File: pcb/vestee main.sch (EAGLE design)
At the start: 45 parts, among them IC1 LD117AS12TR, IC2 FT232RL, Q1 MMBT2222A, Q3 MMBT4403

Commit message: Fixed discovered issues, removed DC jack, added jack for 1-Wire, minor improvements
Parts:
- removed D1, D2: (no value), SparkFun-DiscreteSemi:DIODESMA
- removed JP1: USB-SMD-NS, SparkFun-Connectors:USB-SMD-NS
- removed R17: (no value), rcl:R-EU_R0805
- removed SENS: (no value), SparkFun-Connectors:M05LOCK_LONGPADS
- removed U$3: TACTILE-SWITCH-PTH, GeekAmmo:TACTILE-SWITCH-PTH
- removed VESTEE: (no value), SparkFun-Connectors:M04LOCK_LONGPADS
- added ELECTRODE: (no value), SparkFun-Connectors:M02LOCK_LONGPADS
- added PRPIHERALS: (no value), SparkFun-Connectors:AUDIO-JACK1:1
- added Q2, Q4: MMBT5088, SparkFun-DiscreteSemi:TRANSISTOR_NPNMMBT5088
- added R22, R23, R24, R25: (no value), rcl:R-EU_R0805
- added S2: SWITCH-MOMENTARY-2SMD-4, SparkFun-Electromechanical:SWITCH-MOMENTARY-2SMD-4
- JP2: value 5.5x2.1mm Barrel -> USB-MICROB; device SparkFun-Connectors:POWER_JACKSMD -> SparkFun-Connectors:USB-MICROB
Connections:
- removed net FLOW: R17.2, U$1.GPIO13
- removed net N$20: R12.1, SENS.2
- removed net N$22: R11.1, U$1.REST
- removed net N$23: C4.1, D2.A, IC2.VCC, L1.2
- removed net N$24: U$1.GPIO12, VESTEE.3
- removed net N$25: Q3.C, SENS.5
- removed net N$5: R17.1, VESTEE.4
- new net 1-WIRE: PRPIHERALS.LEFT, R12.1
- new net CBUS_RST: R11.1, R25.2, U$1.REST
- new net N$30: IC2.CBUS2, R22.2
- new net N$31: Q2.C, R24.1
- new net N$32: Q2.B, R23.1
- new net N$33: Q4.B, R22.1
- new net N$34: IC2.CBUS3, R23.2
- new net N$35: Q4.C, R25.1
- net CBUS: now also R24.2; no longer IC2.CBUS4, U$1.GPIO15
- net GND: now also IC2.TEST, JP2.GND, PRPIHERALS.SLEEVE, Q2.E, Q4.E, S2.1, U$1.GPIO15; no longer JP1.GND, JP2.PWR, SENS.1, U$3.1, U$3.2, VESTEE.1
- net N$17: now also ELECTRODE.1, Q3.C; no longer D1.A, JP2.GND, JP2.GNDBREAK
- net N$18: now also S2.2; no longer U$3.3, U$3.4
- net N$2: now also JP2.D+; no longer JP1.D+
- net N$26: now also ELECTRODE.2; no longer SENS.4
- net N$3: now also JP2.D-; no longer JP1.D-
- net N$7: now also JP2.VBUS; no longer JP1.VBUS
- net VCC: now also PRPIHERALS.RIGHT; no longer SENS.3, VESTEE.2
- net VIN: now also C4.1, IC2.VCC, L1.2; no longer D1.C, D2.C

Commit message: Fixed silkscreen
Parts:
- renumbered LED1 to TX, LED2 to RX, LED3 to 3V3
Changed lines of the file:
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@@
 <part name="R3" library="rcl" deviceset="R-EU_" device="R0805"/>
 <part name="R4" library="rcl" deviceset="R-EU_" device="R0805"/>
-<part name="LED1" library="led" deviceset="LED" device="SML0805"/>
-<part name="LED2" library="led" deviceset="LED" device="SML0805"/>
-<part name="LED3" library="led" deviceset="LED" device="SML0805"/>
+<part name="TX" library="led" deviceset="LED" device="SML0805"/>
+<part name="RX" library="led" deviceset="LED" device="SML0805"/>
+<part name="3V3" library="led" deviceset="LED" device="SML0805"/>
 <part name="R5" library="rcl" deviceset="R-EU_" device="R0805"/>
 <part name="GND8" library="supply1" deviceset="GND" device=""/>
@@
 <instance part="R3" gate="G$1" x="170.18" y="58.42" rot="R90"/>
 <instance part="R4" gate="G$1" x="177.8" y="58.42" rot="R90"/>
-<instance part="LED1" gate="G$1" x="170.18" y="68.58"/>
-<instance part="LED2" gate="G$1" x="177.8" y="68.58"/>
-<instance part="LED3" gate="G$1" x="111.76" y="101.6"/>
+<instance part="TX" gate="G$1" x="170.18" y="68.58"/>
+<instance part="RX" gate="G$1" x="177.8" y="68.58"/>
+<instance part="3V3" gate="G$1" x="111.76" y="101.6"/>
 <instance part="R5" gate="G$1" x="104.14" y="106.68" rot="R180"/>
 <instance part="GND8" gate="1" x="111.76" y="91.44"/>
@@
 </segment>
 <segment>
-<pinref part="LED3" gate="G$1" pin="C"/>
+<pinref part="3V3" gate="G$1" pin="C"/>
 <pinref part="GND8" gate="1" pin="GND"/>
 <wire x1="111.76" y1="96.52" x2="111.76" y2="93.98" width="0.1524" layer="91"/>
@@
 <pinref part="IC2" gate="1" pin="VCCIO"/>
 <wire x1="124.46" y1="73.66" x2="129.54" y2="73.66" width="0.1524" layer="91"/>
-<pinref part="LED2" gate="G$1" pin="A"/>
+<pinref part="RX" gate="G$1" pin="A"/>
 <wire x1="177.8" y1="71.12" x2="177.8" y2="83.82" width="0.1524" layer="91"/>
 <wire x1="177.8" y1="83.82" x2="170.18" y2="83.82" width="0.1524" layer="91"/>
 <wire x1="170.18" y1="83.82" x2="124.46" y2="83.82" width="0.1524" layer="91"/>
 <wire x1="124.46" y1="83.82" x2="124.46" y2="81.28" width="0.1524" layer="91"/>
-<pinref part="LED1" gate="G$1" pin="A"/>
+<pinref part="TX" gate="G$1" pin="A"/>
 <wire x1="124.46" y1="81.28" x2="124.46" y2="73.66" width="0.1524" layer="91"/>
 <wire x1="170.18" y1="71.12" x2="170.18" y2="83.82" width="0.1524" layer="91"/>
@@
 <segment>
 <pinref part="R3" gate="G$1" pin="2"/>
-<pinref part="LED1" gate="G$1" pin="C"/>
+<pinref part="TX" gate="G$1" pin="C"/>
 </segment>
 </net>
@@
 <segment>
 <pinref part="R4" gate="G$1" pin="2"/>
-<pinref part="LED2" gate="G$1" pin="C"/>
+<pinref part="RX" gate="G$1" pin="C"/>
 </segment>
 </net>
@@
 <segment>
 <pinref part="R5" gate="G$1" pin="1"/>
-<pinref part="LED3" gate="G$1" pin="A"/>
+<pinref part="3V3" gate="G$1" pin="A"/>
 <wire x1="109.22" y1="106.68" x2="111.76" y2="106.68" width="0.1524" layer="91"/>
 <wire x1="111.76" y1="106.68" x2="111.76" y2="104.14" width="0.1524" layer="91"/>

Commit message: Added new LED to GPIO12, screw holes, bottom layer fixes
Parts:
- removed ELECTRODE: (no value), SparkFun-Connectors:M02LOCK_LONGPADS
- added LED1: (no value), led:LED3MM
- added PAD1, PAD2: (no value), wirepad:SMD2
- added Q5: MMBT5088, SparkFun-DiscreteSemi:TRANSISTOR_NPNMMBT5088
- added R17, R26: (no value), rcl:R-EU_R0805
- C2: device SparkFun-Capacitors:CAP_POLPTH2 -> SparkFun-Capacitors:CAP_POLD
- L1: device SparkFun-Passives:INDUCTOR0805 -> SparkFun-Passives:INDUCTOR1210
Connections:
- new net N$20: R17.1, U$1.GPIO12
- new net N$22: LED1.C, Q5.C
- new net N$23: LED1.A, R26.2
- new net N$5: Q5.B, R17.2
- net GND: now also Q5.E
- net N$17: now also PAD2.P; no longer ELECTRODE.1
- net N$26: now also PAD1.P; no longer ELECTRODE.2
- net VCC: now also R26.1
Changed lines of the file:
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@@
 <layer number="17" name="Pads" color="2" fill="1" visible="no" active="no"/>
 <layer number="18" name="Vias" color="2" fill="1" visible="no" active="no"/>
-<layer number="19" name="Unrouted" color="6" fill="1" visible="no" active="no"/>
+<layer number="19" name="Unrouted" color="14" fill="1" visible="no" active="no"/>
 <layer number="20" name="Dimension" color="15" fill="1" visible="no" active="no"/>
 <layer number="21" name="tPlace" color="7" fill="1" visible="no" active="no"/>
@@
 <part name="GND3" library="supply1" deviceset="GND" device=""/>
 <part name="IC1" library="v-reg" deviceset="LD117A?*" device="S" technology="12TR"/>
-<part name="C2" library="SparkFun-Capacitors" deviceset="CAP_POL" device="PTH2"/>
+<part name="C2" library="SparkFun-Capacitors" deviceset="CAP_POL" device="D"/>
 <part name="C3" library="SparkFun-Capacitors" deviceset="0.33UF-50V-10%(0805)" device="" value="100nF"/>
 <part name="GND4" library="supply1" deviceset="GND" device=""/>
@@
 <part name="R2" library="rcl" deviceset="R-EU_" device="R0805"/>
 <part name="P+2" library="supply1" deviceset="VCC" device=""/>
-<part name="L1" library="SparkFun-Passives" deviceset="INDUCTOR" device="0805"/>
+<part name="L1" library="SparkFun-Passives" deviceset="INDUCTOR" device="1210"/>
 <part name="GND6" library="supply1" deviceset="GND" device=""/>
 <part name="C4" library="SparkFun-Capacitors" deviceset="0.33UF-50V-10%(0805)" device="" value="10nF"/>
@@
 <part name="JP2" library="SparkFun-Connectors" deviceset="USB" device="-MICROB"/>
 <part name="PRPIHERALS" library="SparkFun-Connectors" deviceset="AUDIO-JACK" device="1:1"/>
-<part name="ELECTRODE" library="SparkFun-Connectors" deviceset="M02" device="LOCK_LONGPADS"/>
+<part name="PAD1" library="wirepad" deviceset="SMD2" device=""/>
+<part name="PAD2" library="wirepad" deviceset="SMD2" device=""/>
+<part name="LED1" library="led" deviceset="LED" device="3MM"/>
+<part name="Q5" library="SparkFun-DiscreteSemi" deviceset="TRANSISTOR_NPN" device="MMBT5088" value="MMBT5088"/>
+<part name="GND1" library="supply1" deviceset="GND" device=""/>
+<part name="R17" library="rcl" deviceset="R-EU_" device="R0805"/>
+<part name="R26" library="rcl" deviceset="R-EU_" device="R0805"/>
 </parts>
 <sheets>
@@
 <instance part="JP2" gate="G$1" x="96.52" y="58.42" rot="R180"/>
 <instance part="PRPIHERALS" gate="G$1" x="-17.78" y="73.66" rot="R90"/>
-<instance part="ELECTRODE" gate="G$1" x="-10.16" y="88.9" rot="R90"/>
+<instance part="PAD1" gate="1" x="-12.7" y="93.98" rot="R90"/>
+<instance part="PAD2" gate="1" x="-10.16" y="93.98" rot="R90"/>
+<instance part="LED1" gate="G$1" x="15.24" y="33.02" rot="R180"/>
+<instance part="Q5" gate="G$1" x="10.16" y="40.64" rot="R270"/>
+<instance part="GND1" gate="1" x="5.08" y="30.48"/>
+<instance part="R17" gate="G$1" x="15.24" y="45.72" rot="R180"/>
+<instance part="R26" gate="G$1" x="20.32" y="30.48" rot="R180"/>
 </instances>
 <busses>
@@
 <wire x1="-20.32" y1="81.28" x2="-20.32" y2="78.74" width="0.1524" layer="91"/>
 </segment>
+<segment>
+<pinref part="GND1" gate="1" pin="GND"/>
+<pinref part="Q5" gate="G$1" pin="E"/>
+<wire x1="5.08" y1="33.02" x2="5.08" y2="38.1" width="0.1524" layer="91"/>
+</segment>
 </net>
 <net name="VCC" class="0">
 <segment>
 <pinref part="U$1" gate="G$1" pin="VCC"/>
-<wire x1="22.86" y1="35.56" x2="33.02" y2="35.56" width="0.1524" layer="91"/>
+<wire x1="22.86" y1="35.56" x2="27.94" y2="35.56" width="0.1524" layer="91"/>
 <pinref part="P+1" gate="VCC" pin="VCC"/>
+<wire x1="27.94" y1="35.56" x2="33.02" y2="35.56" width="0.1524" layer="91"/>
 <wire x1="22.86" y1="40.64" x2="22.86" y2="35.56" width="0.1524" layer="91"/>
+<pinref part="R26" gate="G$1" pin="1"/>
+<wire x1="25.4" y1="30.48" x2="27.94" y2="30.48" width="0.1524" layer="91"/>
+<wire x1="27.94" y1="30.48" x2="27.94" y2="35.56" width="0.1524" layer="91"/>
+<junction x="27.94" y="35.56"/>
 </segment>
 <segment>
@@
 <pinref part="R19" gate="G$1" pin="1"/>
 <wire x1="-22.86" y1="96.52" x2="-12.7" y2="96.52" width="0.1524" layer="91"/>
-<pinref part="ELECTRODE" gate="G$1" pin="2"/>
+<pinref part="PAD1" gate="1" pin="P"/>
 </segment>
 </net>
@@
 <net name="N$17" class="0">
 <segment>
-<pinref part="ELECTRODE" gate="G$1" pin="1"/>
 <pinref part="Q3" gate="G$1" pin="C"/>
 <wire x1="-5.08" y1="86.36" x2="-5.08" y2="96.52" width="0.1524" layer="91"/>
 <wire x1="-10.16" y1="96.52" x2="-5.08" y2="96.52" width="0.1524" layer="91"/>
-</segment>
-</net>
+<pinref part="PAD2" gate="1" pin="P"/>
+</segment>
+</net>
+<net name="N$5" class="0">
+<segment>
+<pinref part="Q5" gate="G$1" pin="B"/>
+<pinref part="R17" gate="G$1" pin="2"/>
+<wire x1="10.16" y1="43.18" x2="10.16" y2="45.72" width="0.1524" layer="91"/>
+</segment>
+</net>
+<net name="N$20" class="0">
+<segment>
+<pinref part="U$1" gate="G$1" pin="GPIO12"/>
+<pinref part="R17" gate="G$1" pin="1"/>
+<wire x1="33.02" y1="45.72" x2="20.32" y2="45.72" width="0.1524" layer="91"/>
+</segment>
+</net>
+<net name="N$22" class="0">
+<segment>
+<pinref part="Q5" gate="G$1" pin="C"/>
+<pinref part="LED1" gate="G$1" pin="C"/>
+</segment>
+</net>
+<net name="N$23" class="0">
+<segment>
+<pinref part="LED1" gate="G$1" pin="A"/>
+<pinref part="R26" gate="G$1" pin="2"/>
+</segment>
+</net>

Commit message: Add VCC pads, move silk
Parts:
- added PAD3, PAD4: WIREPAD2,54/1,0, wirepad:WIREPAD2,54/1,0
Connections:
- net GND: now also PAD4.P
- net N$7: now also PAD3.P
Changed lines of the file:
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@@
 <?xml version="1.0" encoding="utf-8"?>
 <!DOCTYPE eagle SYSTEM "eagle.dtd">
-<eagle version="7.4.0">
+<eagle version="7.1.0">
 <drawing>
 <settings>
@@
 <part name="R17" library="rcl" deviceset="R-EU_" device="R0805"/>
 <part name="R26" library="rcl" deviceset="R-EU_" device="R0805"/>
+<part name="PAD3" library="wirepad" deviceset="WIREPAD" device="2,54/1,0"/>
+<part name="PAD4" library="wirepad" deviceset="WIREPAD" device="2,54/1,0"/>
 </parts>
 <sheets>
@@
 <instance part="R17" gate="G$1" x="15.24" y="45.72" rot="R180"/>
 <instance part="R26" gate="G$1" x="20.32" y="30.48" rot="R180"/>
+<instance part="PAD3" gate="G$1" x="109.22" y="68.58" rot="R270"/>
+<instance part="PAD4" gate="G$1" x="101.6" y="68.58" rot="R270"/>
 </instances>
 <busses>
@@
 </segment>
 <segment>
-<wire x1="99.06" y1="58.42" x2="106.68" y2="58.42" width="0.1524" layer="91"/>
+<wire x1="99.06" y1="58.42" x2="101.6" y2="58.42" width="0.1524" layer="91"/>
+<wire x1="101.6" y1="58.42" x2="106.68" y2="58.42" width="0.1524" layer="91"/>
 <wire x1="106.68" y1="58.42" x2="106.68" y2="50.8" width="0.1524" layer="91"/>
 <pinref part="GND6" gate="1" pin="GND"/>
@@
 <junction x="121.92" y="30.48"/>
 <pinref part="JP2" gate="G$1" pin="GND"/>
+<pinref part="PAD4" gate="G$1" pin="P"/>
+<wire x1="101.6" y1="66.04" x2="101.6" y2="58.42" width="0.1524" layer="91"/>
+<junction x="101.6" y="58.42"/>
 </segment>
 <segment>
@@
 <wire x1="109.22" y1="55.88" x2="99.06" y2="55.88" width="0.1524" layer="91"/>
 <pinref part="JP2" gate="G$1" pin="VBUS"/>
-</segment>
-</net>
+<pinref part="PAD3" gate="G$1" pin="P"/>
+<wire x1="109.22" y1="66.04" x2="109.22" y2="55.88" width="0.1524" layer="91"/>
+<junction x="109.22" y="55.88"/>
+</segment>
+</net>

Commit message: Version 2, all issues fixed
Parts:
- removed 3V3, RX, TX: (no value), led:LEDSML0805
- removed LED1: (no value), led:LED3MM
- removed PAD3, PAD4: WIREPAD2,54/1,0, wirepad:WIREPAD2,54/1,0
- removed Q2, Q4, Q5: MMBT5088, SparkFun-DiscreteSemi:TRANSISTOR_NPNMMBT5088
- removed R13, R17, R22, R23, R24, R25, R26, R4, R5: (no value), rcl:R-EU_R0805
- added DBG_TX, DBG_TX1, PAD5: (no value), wirepad:SMD2
- PRPIHERALS: value (none) -> AUDIO-JACK-2.5-CUI; device SparkFun-Connectors:AUDIO-JACK1:1 -> SparkFun-Connectors:AUDIO-JACK-2.5-CUI
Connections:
- removed net CBUS: R13.1, R24.2, U$1.GPIO0
- removed net CBUS_RST: R11.1, R25.2, U$1.REST
- removed net N$11: IC2.CBUS0, R3.1
- removed net N$12: IC2.CBUS1, R4.1
- removed net N$13: R3.2, TX.C
- removed net N$14: R4.2, RX.C
- removed net N$20: R17.1, U$1.GPIO12
- removed net N$22: LED1.C, Q5.C
- removed net N$23: LED1.A, R26.2
- removed net N$30: IC2.CBUS2, R22.2
- removed net N$31: Q2.C, R24.1
- removed net N$32: Q2.B, R23.1
- removed net N$33: Q4.B, R22.1
- removed net N$34: IC2.CBUS3, R23.2
- removed net N$35: Q4.C, R25.1
- removed net N$8: 3V3.A, R5.1
- new net DTR: IC2.!DTR, R3.2, U$1.GPIO0
- new net RTS: IC2.!RTS, R11.1, U$1.REST
- net FLED: now also U$1.GPIO12; no longer U$1.GPIO2
- net GND: now also DBG_TX1.P, PAD5.P; no longer 3V3.C, PAD4.P, Q2.E, Q4.E, Q5.E
- net N$5: now also DBG_TX.P, U$1.GPIO2; no longer Q5.B, R17.2
- net N$7: no longer PAD3.P
- net VCC: now also R3.1; no longer R13.2, R26.1, R5.2, RX.A, TX.A
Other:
- moved on the sheet: R3

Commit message: pcb rev3
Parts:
- removed C6: 100nF, SparkFun-Capacitors:0.33UF-50V-10%(0805)
- removed DBG_TX, DBG_TX1, PAD1, PAD2, PAD5: (no value), wirepad:SMD2
- removed IC2: FT232RL, ftdichip:FT232RL
- removed LED4: (no value), led:LEDSML0805
- removed R16, R18, R19: (no value), rcl:R-EU_R0805
- added C1: (no value), SparkFun-Passives:CAP_POL3528
- added C7, C8: 100nF, rcl:C-EUC0603
- added D1, D2, D4, D5, D6, D7, D8: KPBA-3010ESGC, SparkFun-LED:APA3010SF4C
- added IC3: CP210X_USB_UART, SparkFun-DigitalIC:CP210X_USB_UART
- added PRPIHERALS1: AUDIO-JACK-2.5-CUI, SparkFun-Connectors:AUDIO-JACK-2.5-CUI
- added R30, R31: 12k, rcl:R-EU_R0603
- added U$3, U$4: SCT2024CSSG, vestee:SCT2024CSSG
- C2: value (none) -> 100nF; device SparkFun-Capacitors:CAP_POLD -> rcl:C-EUC0603
- C3: device SparkFun-Capacitors:0.33UF-50V-10%(0805) -> rcl:C-EUC0603
- C4: value 10nF -> 10n; device SparkFun-Capacitors:0.33UF-50V-10%(0805) -> rcl:C-EUC0603
- C5: value 100nF -> 100n; device SparkFun-Capacitors:0.33UF-50V-10%(0805) -> rcl:C-EUC0603
- D3: value (none) -> KPBA-3010ESGC; device diode:ZENER-DIODESOD80C -> SparkFun-LED:APA3010SF4C
- Q3: value MMBT4403 -> MMBT2222A; device SparkFun-DiscreteSemi:TRANSISTOR_PNPMMBT4403 -> SparkFun-DiscreteSemi:TRANSISTOR_NPNMMBT2222A
- R1, R12, R2, R20, R21, R3, R7: device rcl:R-EU_R0805 -> rcl:R-EU_R0603
- R10, R11, R6, R9: value (none) -> 12k; device rcl:R-EU_R0805 -> rcl:R-EU_R0603
- R14, R8: value (none) -> 470R; device rcl:R-EU_R0805 -> rcl:R-EU_R0603
- R15: value (none) -> 470; device rcl:R-EU_R0805 -> rcl:R-EU_R0603
- U$2: value (none) -> KCDA02-103; device DHT11:DHT11 -> vestee:KCDA02-103
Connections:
- net N$19 renamed SWITCH
- removed net ELECTRODE: R15.1, U$1.GPIO4
- removed net FLED: R6.2, U$1.GPIO12
- removed net N$1: R1.1, R18.1, U$1.GPIO14
- removed net N$10: Q1.B, R14.1, R6.1
- removed net N$16: LED4.C, Q1.C
- removed net N$17: PAD2.P, Q3.C
- removed net N$21: R10.1, U$1.CH_PD
- removed net N$26: PAD1.P, R19.1
- removed net N$27: Q3.B, R15.2, R16.1
- removed net N$4: R12.2, R2.1, U$1.GPIO16
- removed net N$6: R18.2, U$2.DATA
- new net A1: U$2.A1, U$3.O2
- new net A2: U$2.A2, U$3.O6
- new net B1: U$2.B1, U$3.O3
- new net B2: U$2.B2, U$3.O7
- new net C1: U$2.C1, U$3.O13
- new net C2: U$2.C2, U$3.O9
- new net CH_PD: R11.1, U$1.CH_PD
- new net CLK: U$1.GPIO13, U$3.CLK
- new net D1: U$2.D1, U$3.O14
- new net D1G: D1.3, U$4.O7
- new net D1R: D1.2, U$4.O6
- new net D2: U$2.D2, U$3.O10
- new net D2G: D2.3, U$4.O5
- new net D2R: D2.2, U$4.O4
- new net D3G: D3.3, U$4.O3
- new net D3R: D3.2, U$4.O2
- new net D4G: D4.3, U$4.O1
- new net D4R: D4.2, U$4.O0
- new net D5G: D5.3, U$4.O14
- new net D5R: D5.2, U$4.O15
- new net D6G: D6.3, U$4.O13
- new net D6R: D6.2, U$4.O12
- new net D7G: D7.3, U$4.O11
- new net D7R: D7.2, U$4.O10
- new net D8G: D8.3, U$4.O9
- new net D8R: D8.2, U$4.O8
- new net DP1: U$2.DP1, U$3.O12
- new net DP2: U$2.DP2, U$3.O8
- new net E1: U$2.E1, U$3.O15
- new net E2: U$2.E2, U$3.O11
- new net F1: U$2.F1, U$3.O1
- new net F2: U$2.F2, U$3.O5
- new net G1: U$2.G1, U$3.O0
- new net G2: U$2.G2, U$3.O4
- new net GPIO0: Q1.C, R30.1, R7.2, U$1.GPIO0
- new net GPIO16: R15.1, U$1.GPIO16
- new net GPIO2: R31.1, U$1.GPIO2
- new net JACK: PRPIHERALS.LEFT, PRPIHERALS1.LEFT, R12.1
- new net LA/: U$1.GPIO4, U$3.LA/
- new net N$14: IC3.!RST, R6.2
- new net REST: C2.1, Q3.C, R10.1, R15.2, U$1.REST
- new net SDI: U$1.GPIO12, U$4.SDI
- new net SDO: U$3.SDI, U$4.SDO
- new net TXD: IC3.TXD, R14.2
- net 1-WIRE: now also R12.2, R2.1, U$1.GPIO15; no longer PRPIHERALS.LEFT, R12.1
- net ADC: no longer D3.C, R19.2
- net DTR: now also IC3.DTR, Q1.E, R1.1; no longer IC2.!DTR, R3.2, U$1.GPIO0
- net FTDI_RXD: now also IC3.RXD; no longer IC2.RXD
- net FTDI_TXD: now also R14.1; no longer IC2.TXD
- net GND: now also C1.-, C2.2, C7.2, C8.2, IC3.GND, IC3.GND@EXP, IC3.GND@M, PRPIHERALS1.SLEEVE, U$3.GND, U$4.GND; no longer C2.-, C6.1, D3.A, DBG_TX1.P, IC2.GND, IC2.GND@1, IC2.GND@2, IC2.GND@A, IC2.TEST, PAD5.P, Q1.E, R14.2, U$1.GPIO15, U$2.GND
- net N$15: now also Q1.B, R3.2; no longer LED4.A, R7.1
- net N$28: now also IC3.D+; no longer IC2.USBDP
- net N$29: now also IC3.D-; no longer IC2.USBDM
- net N$5: now also Q3.B, R1.2; no longer DBG_TX.P, U$1.GPIO2
- net N$9: now also IC3.VDD; no longer IC2.3V3OUT
- net RTS: now also IC3.RTS, Q3.E, R3.1; no longer IC2.!RTS, R11.1, U$1.REST
- net VCC: now also C1.+, C7.1, C8.1, D1.COM, D2.COM, D3.COM, D4.COM, D5.COM, D6.COM, D7.COM, D8.COM, PRPIHERALS1.RIGHT, R30.2, R31.2, R6.1, R7.1, U$2.V1, U$2.V2, U$2.V3, U$2.V4, U$3.VDD, U$4.VDD; no longer C2.+, C6.2, IC2.VCCIO, Q3.E, R1.2, R16.2, R3.1, R7.2, U$2.VCC
- net VIN: now also IC3.REGIN, IC3.VBUS; no longer IC2.VCC
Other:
- moved on the sheet: C4, PRPIHERALS, Q1, Q3, R1, R10, R11, R12, R14, R15, R2, R21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

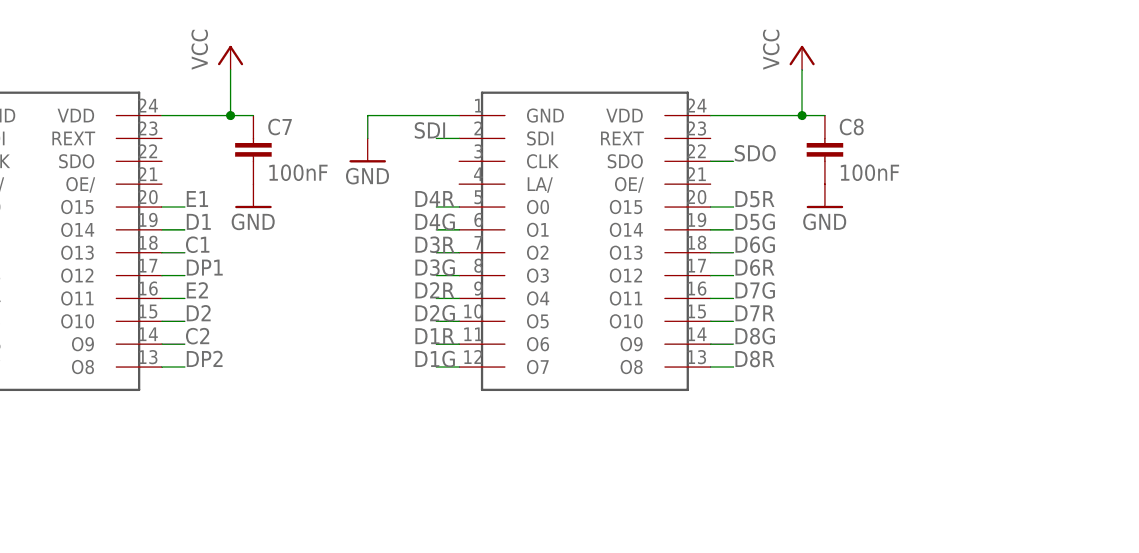
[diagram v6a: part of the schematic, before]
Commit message: Added current setting resistors for LED drivers
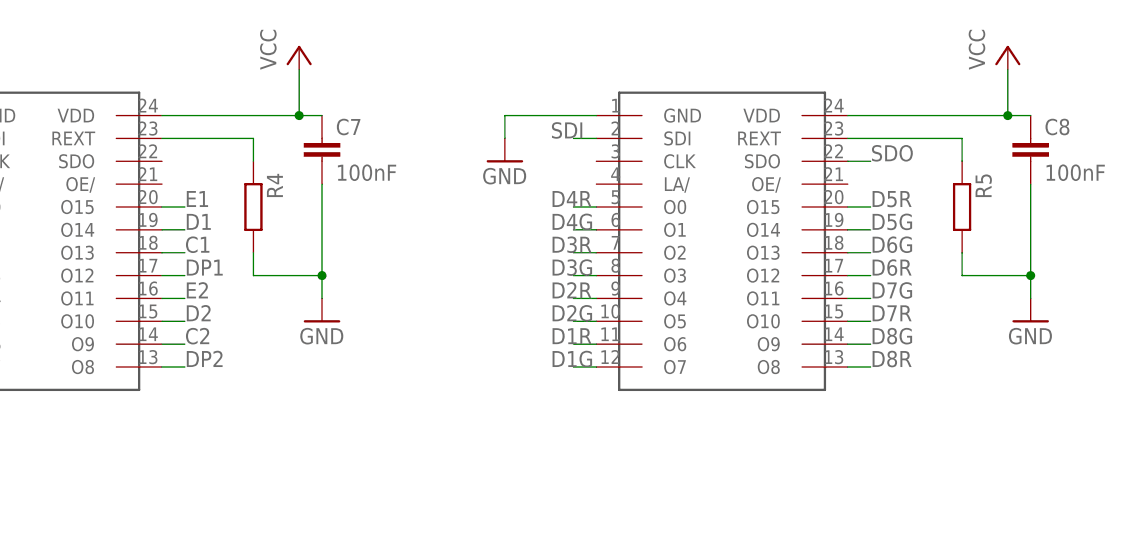
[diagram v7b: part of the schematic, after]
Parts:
- added R4, R5: (no value), rcl:R-EU_R0603
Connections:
- new net N$1: R4.1, U$3.REXT
- new net N$4: R5.1, U$4.REXT
- net GND: now also R4.2, R5.2
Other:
- moved on the sheet: C7, C8
